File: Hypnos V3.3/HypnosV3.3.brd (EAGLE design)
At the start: 25.6 x 52.4 mm, 38 parts, among them Q1 DMN65D8L-7, Q2 DMN65D8L-7

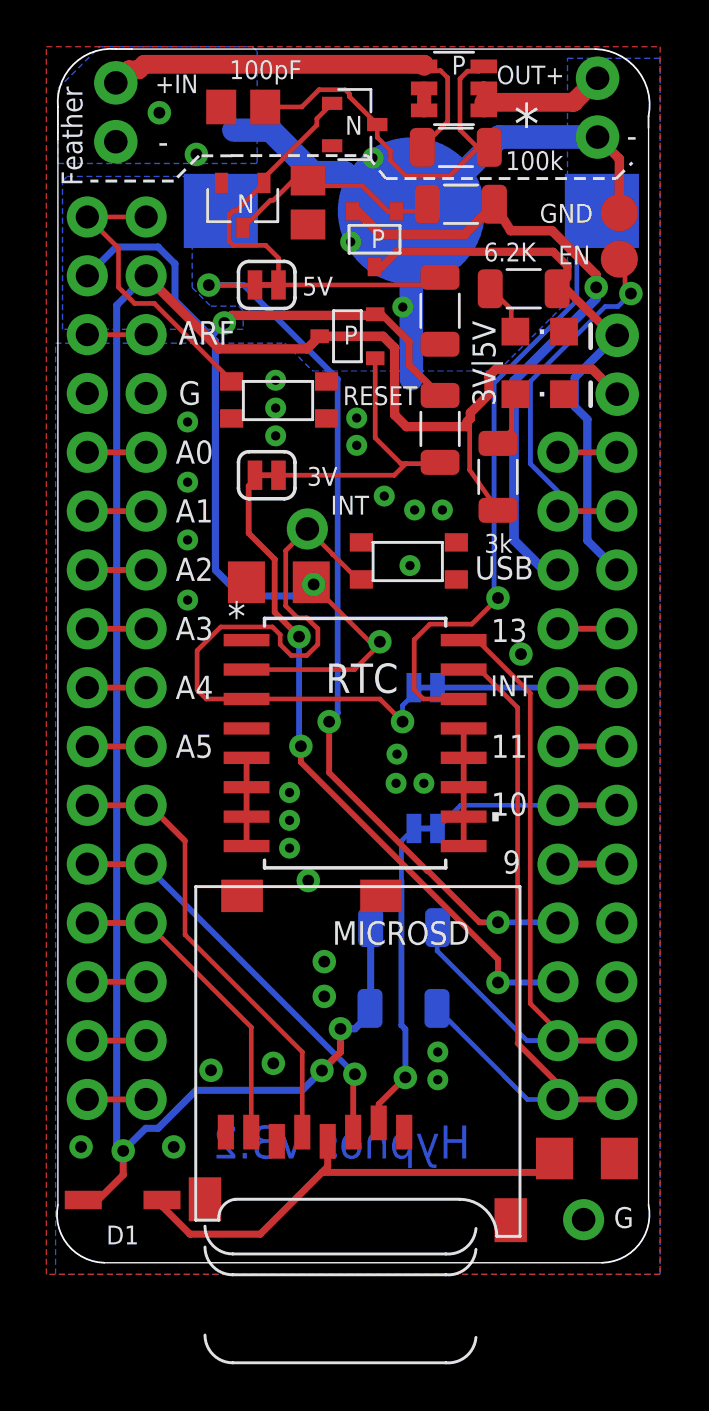
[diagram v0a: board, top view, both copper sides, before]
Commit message: Hypnos V3.3 Update
Changed SD pin from GPIO10 to GPIO9 and removed extra capacitors from design
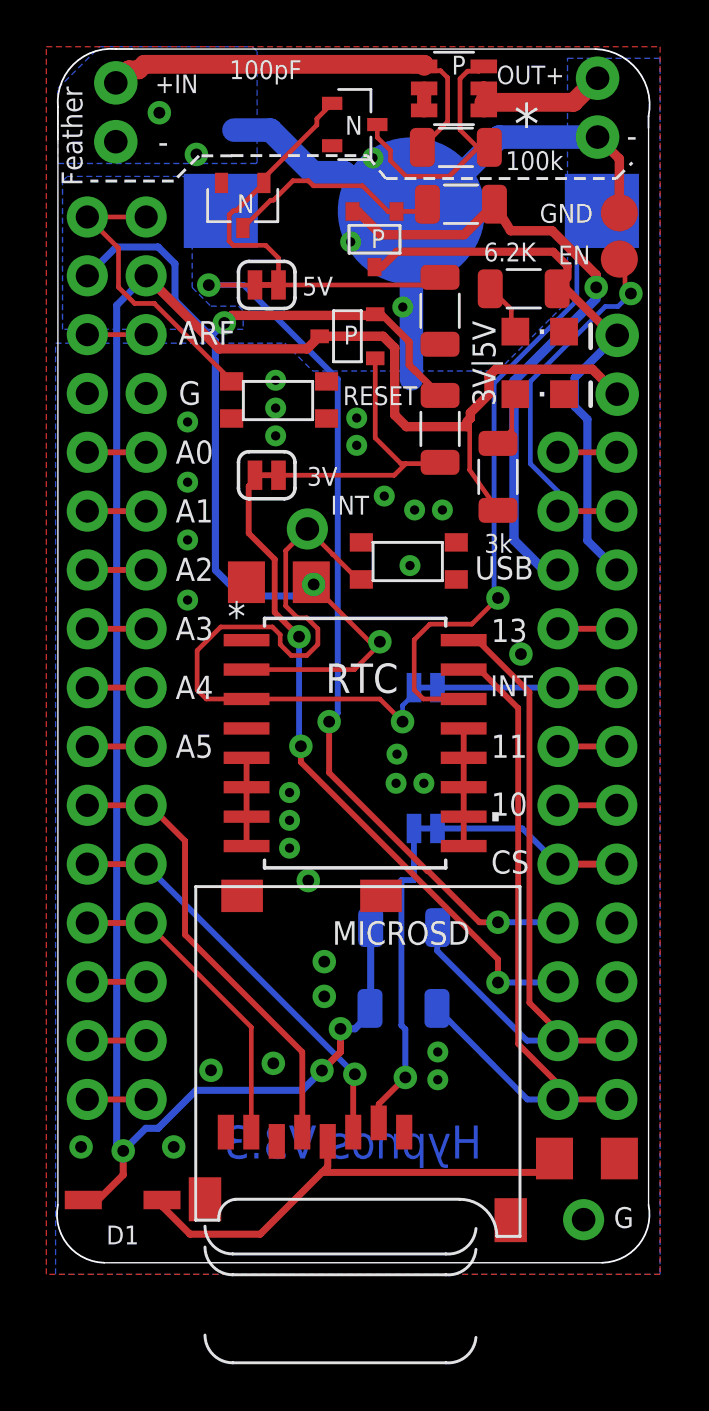
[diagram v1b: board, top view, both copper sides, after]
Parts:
- removed C2, C4: 100pF, resistor:C0805
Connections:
- removed net N$11: CS.1, FEATHERWING.22, MS2.22
- new net 10: FEATHERWING.22, MS2.22
- net 9: now also CS.1
- net GND: no longer C2.2, C4.2
- net N$10: no longer C2.1
- net N$15: no longer C4.1
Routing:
- net N$11: track 8.16 -> 0.00 mm
- net N$15: track 17.7 -> 11.9 mm
- net 9: track 2.54 -> 8.38 mm
- net 10: track 0.00 -> 2.54 mm
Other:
- board text added: "Bryson Goto"
- board text added: "CS"
- board text added: "Hypnos V3.3"
- board text added: "OPEnS Lab"
- board text removed: "9"
- board text removed: "Bao Nguyen"
- board text removed: "Hypnos V3.2"
- board text removed: "OpenSlab"

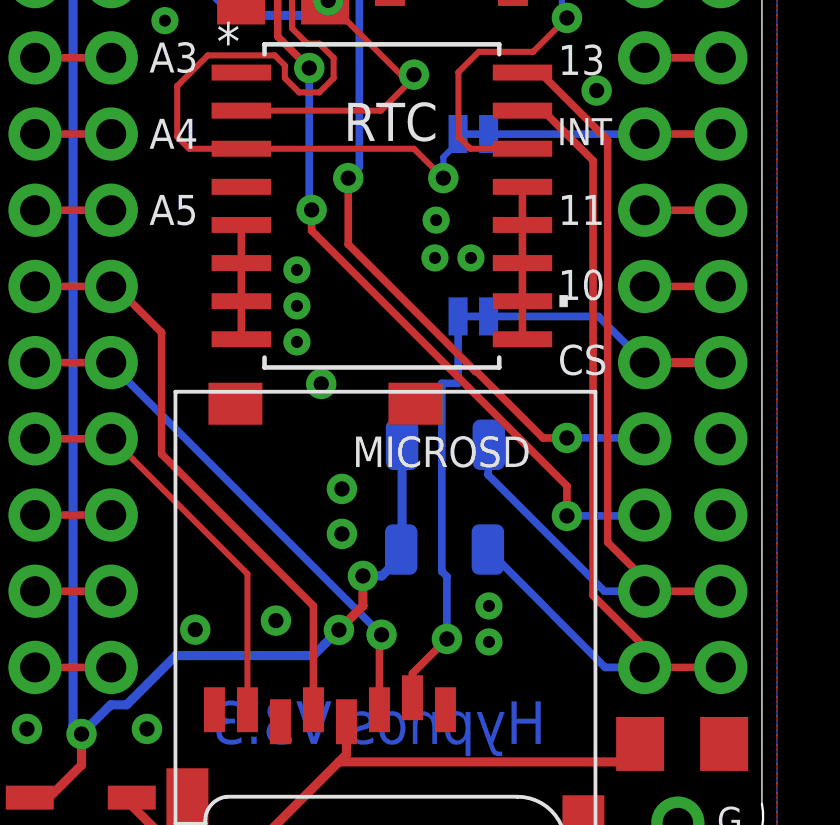
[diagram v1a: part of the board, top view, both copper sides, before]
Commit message: Hypnos V3.3 Update
Switched SD pin from pin 9 to pin 11 due to Feather pin issues, updated BOM with in-stock parts from Digikey
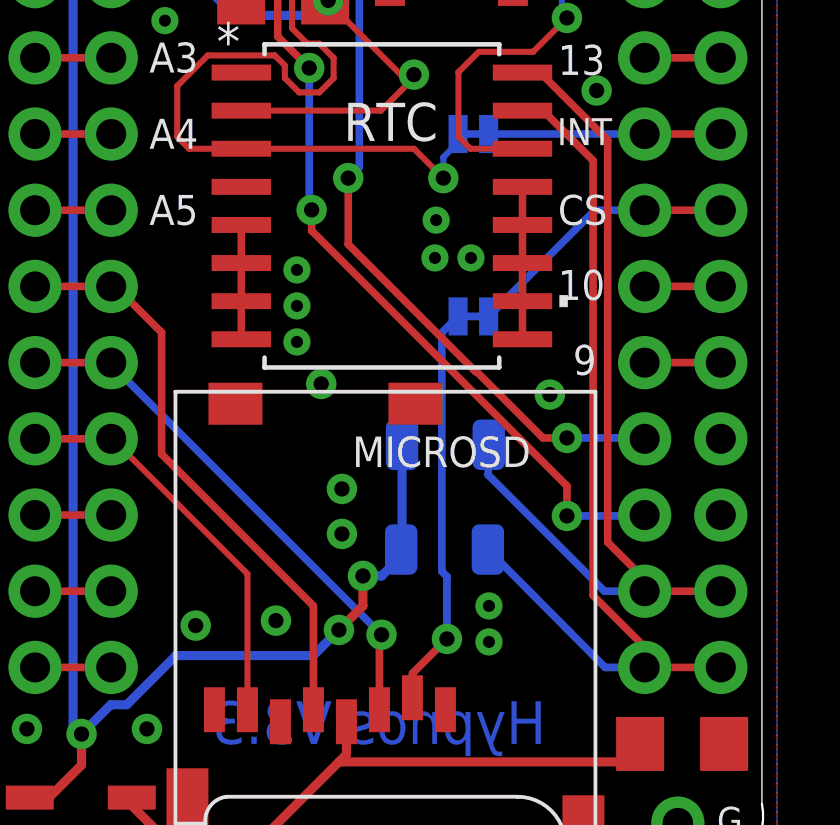
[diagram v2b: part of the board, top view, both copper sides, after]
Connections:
- net 11: now also CS.1
- net 9: no longer CS.1
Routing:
- net 11: track 2.54 -> 9.21 mm
- net 9: track 8.38 -> 2.54 mm
- net GND: vias 34 -> 35
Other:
- board text added: "9"
- board text removed: "11"
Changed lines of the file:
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@@
 <text x="20.62" y="7.06" size="1.016" layer="22" ratio="10" rot="MR0">SDA</text>
 <text x="20.62" y="9.6" size="1.016" layer="22" ratio="10" rot="MR0">SCL</text>
-<text x="20.62" y="17.22" size="1.016" layer="22" ratio="10" rot="MR0">CS</text>
+<text x="20.62" y="17.22" size="1.016" layer="22" ratio="10" rot="MR0">9</text>
 <text x="20.62" y="19.76" size="1.016" layer="22" ratio="10" rot="MR0">10</text>
-<text x="20.62" y="22.3" size="1.016" layer="22" ratio="10" rot="MR0">11</text>
+<text x="20.62" y="22.3" size="1.016" layer="22" ratio="10" rot="MR0">CS</text>
 <text x="20.62" y="24.84" size="1.016" layer="22" ratio="10" rot="MR0">INT</text>
 <text x="20.62" y="27.38" size="1.016" layer="22" ratio="10" rot="MR0">13</text>
@@
 <text x="19.7" y="27.3" size="1" layer="25" ratio="10">13</text>
 <text x="19.67" y="24.96" size="0.9" layer="25" ratio="10">INT</text>
-<text x="19.7" y="22.3" size="1" layer="25" ratio="10">11</text>
+<text x="19.7" y="22.3" size="1" layer="25" ratio="10">CS</text>
 <text x="19.7" y="19.8" size="1" layer="25" ratio="10">10</text>
-<text x="19.7" y="17.3" size="1" layer="25" ratio="10">CS</text>
+<text x="20.2" y="17.3" size="1" layer="25" ratio="10">9</text>
 <wire x1="24.5" y1="0.5" x2="26.5" y2="3" width="0.0762" layer="20" curve="100"/>
 <wire x1="3" y1="0.5" x2="1" y2="3" width="0.0762" layer="20" curve="-100"/>
@@
 <contactref element="U$2" pad="3"/>
 <via x="20.99" y="26.78" extent="1-16" drill="0.508"/>
-<via x="7.61" y="8.81" extent="1-16" drill="0.508"/>
+<via x="7.625" y="8.945" extent="1-16" drill="0.508"/>
 <via x="12.5" y="13.5" extent="1-16" drill="0.508"/>
 <wire x1="16.26" y1="45.91" x2="16.26" y2="38.66" width="1.016" layer="16"/>
@@
 <via x="6.6" y="31.705" extent="1-16" drill="0.4"/>
 <via x="6.6" y="29.11" extent="1-16" drill="0.4"/>
+<via x="19.43" y="16.645" extent="1-16" drill="0.508"/>
 <wire x1="17.5" y1="40.155" x2="16.26" y2="38.66" width="0" layer="19" extent="1-16"/>
 <wire x1="13.64" y1="44.575" x2="16.26" y2="45.91" width="0" layer="19" extent="16-16"/>
@@
 <wire x1="16" y1="8.5" x2="16" y2="10.58" width="0.254" layer="16"/>
 <wire x1="16" y1="10.58" x2="15.83" y2="10.75" width="0.254" layer="16"/>
-<wire x1="15.83" y1="17.019934375" x2="15.83" y2="10.75" width="0.254" layer="16"/>
-<wire x1="15.83" y1="17.019934375" x2="16.372" y2="17.019934375" width="0.254" layer="16"/>
-<wire x1="16.372" y1="19.25" x2="16.372" y2="17.019934375" width="0.254" layer="16"/>
+<wire x1="16.372" y1="19.25" x2="15.83" y2="18.708" width="0.254" layer="16"/>
+<wire x1="15.83" y1="18.708" x2="15.83" y2="10.75" width="0.254" layer="16"/>
 </signal>
 <signal name="SCL">
@@
 <contactref element="FEATHERWING" pad="21"/>
 <contactref element="MS2" pad="21"/>
-<wire x1="22.59" y1="17.71" x2="25.13" y2="17.71" width="0.3048" layer="1"/>
-<contactref element="CS" pad="1"/>
-<wire x1="17.388" y1="19.25" x2="21.05" y2="19.25" width="0.254" layer="16"/>
-<wire x1="21.05" y1="19.25" x2="22.59" y2="17.71" width="0.254" layer="16"/>
+<wire x1="25.13" y1="17.71" x2="22.59" y2="17.71" width="0.254" layer="1"/>
 </signal>
 <signal name="EN">
@@
 <contactref element="MS2" pad="23"/>
 <wire x1="22.59" y1="22.79" x2="25.13" y2="22.79" width="0.254" layer="1"/>
+<contactref element="CS" pad="1"/>
+<wire x1="17.388" y1="19.25" x2="20.928" y2="22.79" width="0.254" layer="16"/>
+<wire x1="20.928" y1="22.79" x2="22.59" y2="22.79" width="0.254" layer="16"/>
 </signal>
 <signal name="A4">
@@
 </signals>
 <mfgpreviewcolors>
-<mfgpreviewcolor name="soldermaskcolor" color="0xC855007F"/>
+<mfgpreviewcolor name="soldermaskcolor" color="0xC800AA00"/>
 <mfgpreviewcolor name="silkscreencolor" color="0xFFFFFFFF"/>
 <mfgpreviewcolor name="backgroundcolor" color="0xFF282828"/>
